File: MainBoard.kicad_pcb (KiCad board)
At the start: 4 copper layers, 110 x 100 mm, 99 parts, among them J1 USB B Mini, J5 Audio Out Port, P1 CARTRIDGE_SLOT, P2 FRONT_PANEL_CONNECTOR, P4 Multi AV Out, Q1 2SC4699, SW1 RESET, U1 S-CPU, U11 PST529D, U13 S-SMP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

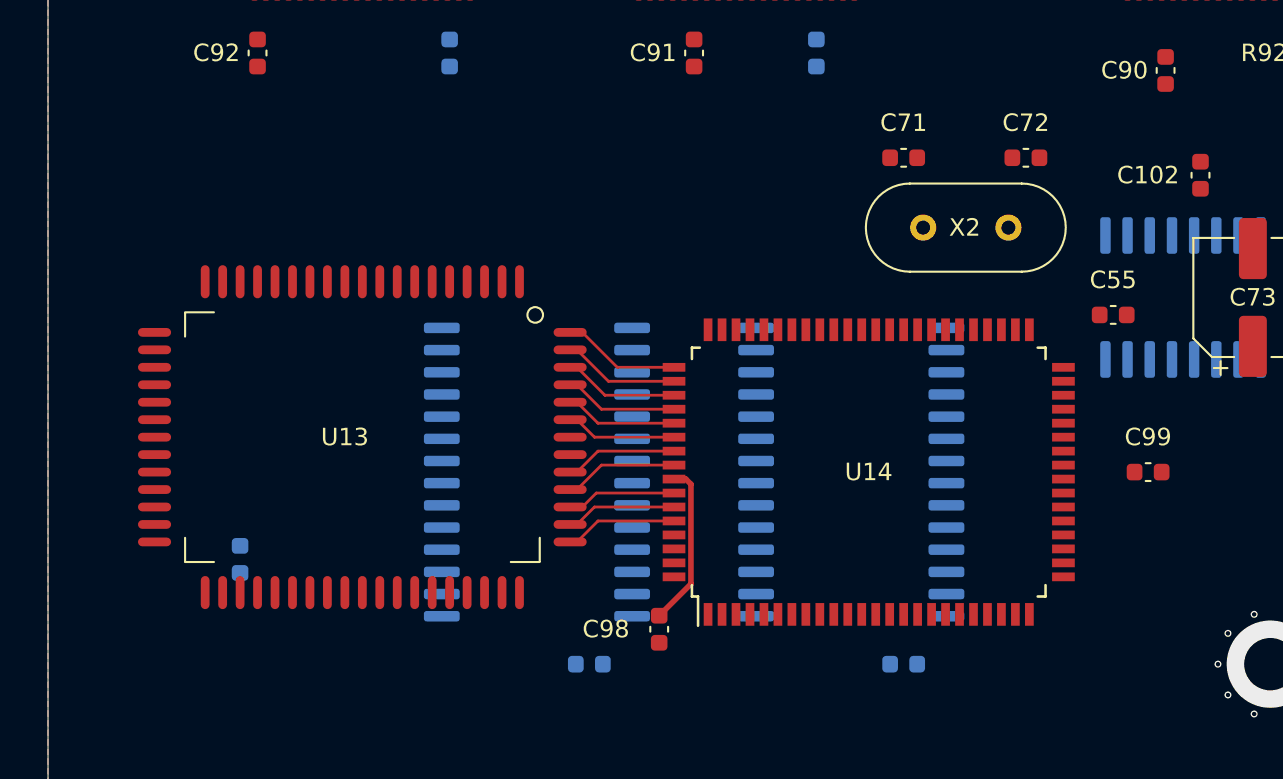
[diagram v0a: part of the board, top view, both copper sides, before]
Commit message: Sound section wiring completed
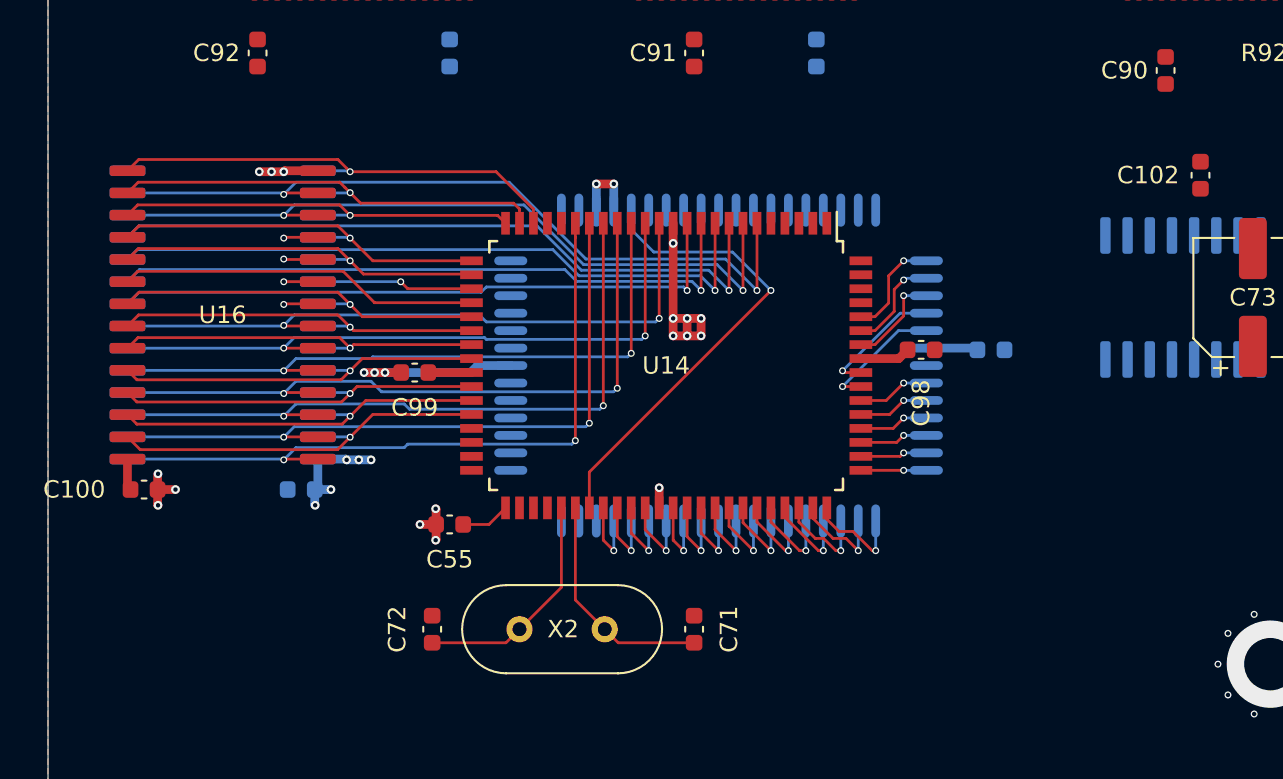
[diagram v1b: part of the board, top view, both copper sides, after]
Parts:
- C100, U16: moved to F.Cu
- U13: moved to B.Cu
- moved C97 44.6 mm to (74.0, 118.0), turned to 0 degrees
- moved C100 44.6 mm to (25.5, 126.0), turned to 180 degrees
- moved C72 43.4 mm to (42.0, 134.0), turned to 270 degrees
- moved C99 42.4 mm to (41.0, 119.3), turned to 180 degrees
- moved C55 39.8 mm to (43.0, 128.0), turned to 180 degrees
- moved U16 37.1 mm to (30.0, 116.0), turned to 180 degrees
- moved X2 36.2 mm to (47.0, 134.0), turned to 0 degrees
- moved C71 29.5 mm to (57.0, 134.0), turned to 270 degrees
- moved C98 21.9 mm to (70.0, 118.0), turned to 180 degrees
- moved U13 20.8 mm to (58.4, 118.9), turned to 90 degrees
- moved U15 20.1 mm to (30.0, 116.0)
- moved C101 19.3 mm to (34.5, 126.0)
- moved U14 13.1 mm to (55.4, 118.9), turned to 270 degrees
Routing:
- net /MD2: track 0.00 -> 44.8 mm, vias 0 -> 2
- net /MD1: track 0.00 -> 43.3 mm, vias 0 -> 2
- net /MD0: track 0.00 -> 42.1 mm, vias 0 -> 2
- net /MA0: track 0.00 -> 40.7 mm, vias 0 -> 2
- net /MA14: track 0.00 -> 40.5 mm, vias 0 -> 2
- net /MA7: track 0.00 -> 40.2 mm, vias 0 -> 2
- net /MA12: track 0.00 -> 40.2 mm, vias 0 -> 2
- net /MA6: track 0.00 -> 40.1 mm, vias 0 -> 2
- net /MA1: track 0.00 -> 39.4 mm, vias 0 -> 2
- net /MA5: track 0.00 -> 38.7 mm, vias 0 -> 2
- net /MA4: track 0.00 -> 38.4 mm, vias 0 -> 2
- net /MA3: track 0.00 -> 38.4 mm, vias 0 -> 2
- net /MA2: track 0.00 -> 38.3 mm, vias 0 -> 2
- net GND: track 0.00 -> 31.2 mm, vias 15 -> 35
- net /MD3: track 0.00 -> 27.4 mm, vias 0 -> 1
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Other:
- net class Power: trace_width 0.32 -> 0.5

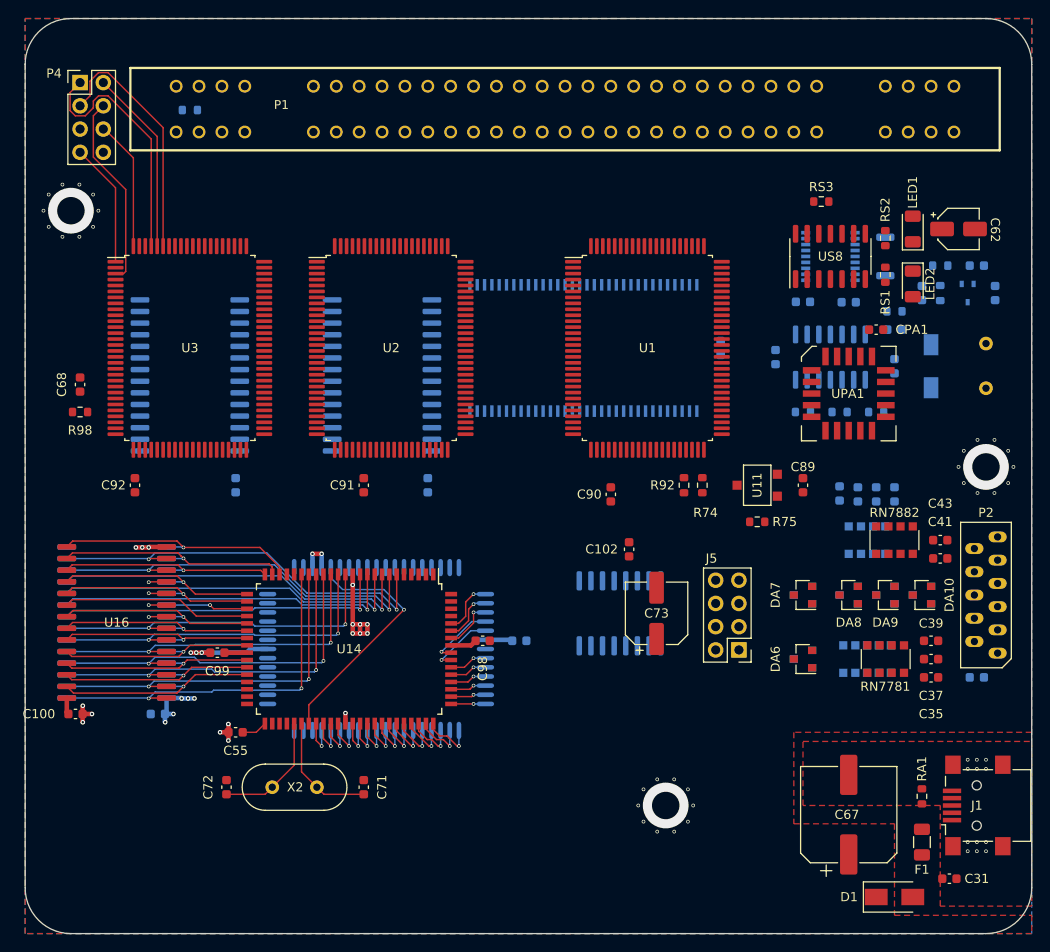
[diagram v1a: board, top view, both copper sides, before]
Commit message: Sound section connected to the main CPU now
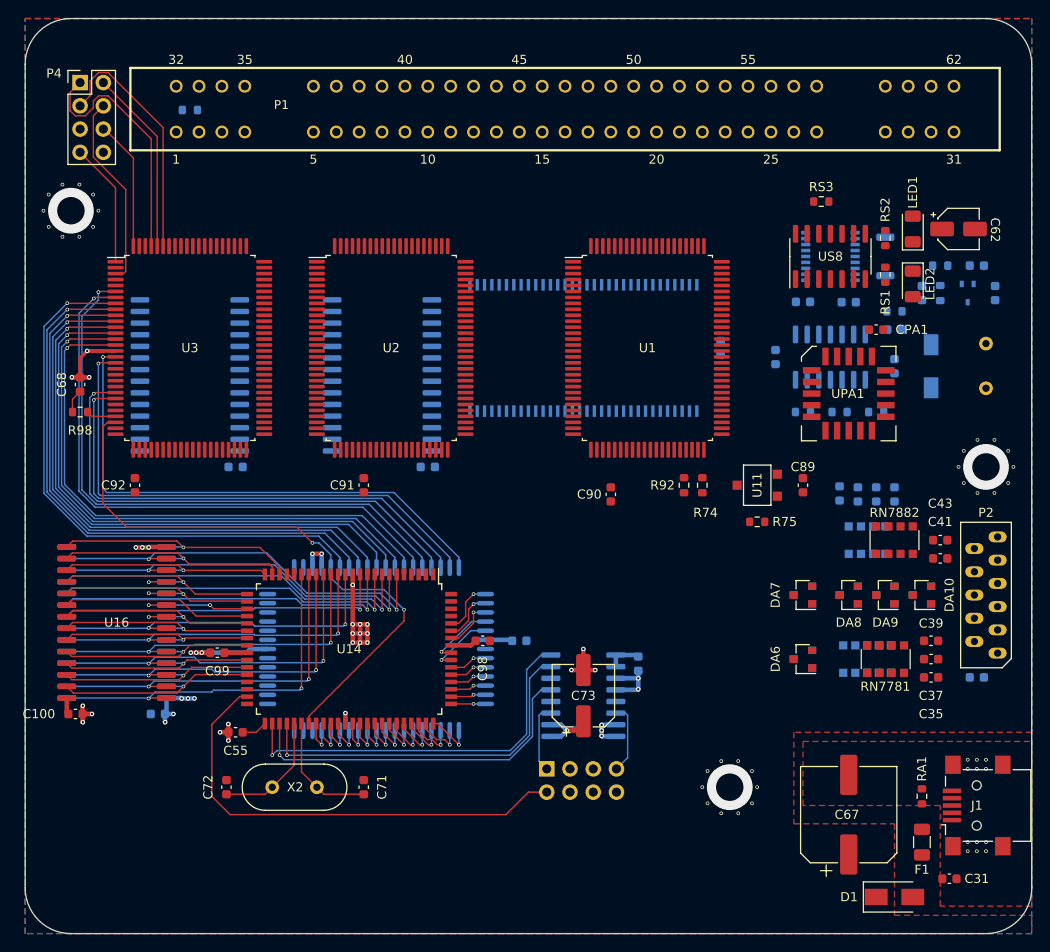
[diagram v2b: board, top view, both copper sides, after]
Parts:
- C102, J5: moved to B.Cu
- moved J5 24.7 mm to (77.0, 132.0), turned to 270 degrees
- moved C102 12.5 mm to (87.0, 120.5)
- moved C73 12.0 mm to (81.0, 124.0)
- moved U17 9.85 mm to (81.0, 124.0), turned to 180 degrees
- moved C93 2.00 mm to (43.0, 99.0), turned to 0 degrees
- moved C94 2.00 mm to (64.0, 99.0), turned to 0 degrees
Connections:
- J5 pad 1: /~MUTE -> /AUDIO_LOUT
- J5 pad 2: /AUDIO_LOUT -> /~MUTE
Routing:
- net /~PAWR: track 0.00 -> 65.6 mm, vias 0 -> 1
- net /~PARD: track 0.00 -> 64.8 mm, vias 0 -> 1
- net /D7: track 0.00 -> 63.5 mm, vias 0 -> 1
- net /D6: track 0.00 -> 63.2 mm, vias 0 -> 1
- net /D5: track 0.00 -> 63.0 mm, vias 0 -> 1
- net /D3: track 0.00 -> 62.9 mm, vias 0 -> 1
- net /D4: track 0.00 -> 62.8 mm, vias 0 -> 1
- net /D2: track 0.00 -> 62.6 mm, vias 0 -> 1
- net /D1: track 0.00 -> 62.2 mm, vias 0 -> 1
- net /D0: track 0.00 -> 62.0 mm, vias 0 -> 1
- net /PA7: track 0.00 -> 58.9 mm, vias 0 -> 1
- net /PA6: track 0.00 -> 58.5 mm, vias 0 -> 1
- net /PA1: track 0.00 -> 54.9 mm, vias 0 -> 1
- net /PA0: track 0.00 -> 54.6 mm, vias 0 -> 1
- net /~MUTE: track 0.00 -> 51.4 mm
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
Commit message: WIP, needs rewiring
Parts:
- removed C94: 0.1uF, Capacitor_SMD:C_0603_1608Metric
- C89, R75: moved to B.Cu
- U6: footprint SNES:SOP-64_10.8x28mm_P0.8mm -> SNES:SOP-64_10.9x26.5mm_P0.8mm
- moved C90 31.9 mm to (91.6, 71.0), turned to 270 degrees
- moved C95 26.2 mm to (70.5, 91.9), turned to 90 degrees
- moved U4 6.08 mm to (37.0, 83.0)
- moved R75 5.94 mm to (95.0, 101.8)
- moved C89 5.28 mm to (100.0, 102.7), turned to 0 degrees
- moved U6 4.43 mm to (82.9, 82.0)
- moved C93 4.31 mm to (46.0, 95.9), turned to 180 degrees
- moved RS3 3.16 mm to (110.0, 71.0)
- moved C62 3.00 mm to (125.0, 73.0), turned to 180 degrees
- moved LED1 3.00 mm to (120.0, 73.0)
- moved LED2 3.00 mm to (120.0, 79.0)
- moved RS1 3.00 mm to (117.0, 78.0)
- moved RS2 3.00 mm to (117.0, 74.0)
- moved UPA1 3.00 mm to (113.0, 91.0)
- moved US8 3.00 mm to (111.0, 76.0)
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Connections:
- U3 pad 34: /XIN -> /~RESET
- U8 pad 10: /XIN -> /~RESET
- US8 pad 11: /XIN -> /~RESET
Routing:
- net /PA7: track 58.9 -> 189.9 mm, vias 1 -> 6
- net /PA0: track 54.6 -> 180.2 mm, vias 1 -> 5
- net /PA1: track 54.9 -> 177.1 mm, vias 1 -> 5
- net /PA3: track 0.00 -> 109.3 mm, vias 0 -> 4
- net /PA5: track 0.00 -> 104.9 mm, vias 0 -> 3
- net /~RAMSEL: track 0.00 -> 104.9 mm, vias 0 -> 2
- net /PA2: track 0.00 -> 103.7 mm, vias 0 -> 4
- net /PA4: track 0.00 -> 101.8 mm, vias 0 -> 3
- net /~RESOUT1: track 65.9 -> 165.3 mm, vias 2 -> 4
- net /D7: track 63.5 -> 150.6 mm, vias 1 -> 4
- net /REFRESH: track 0.00 -> 84.9 mm, vias 0 -> 2
- net /PA6: track 58.5 -> 139.5 mm, vias 1 -> 4
- net /D6: track 63.2 -> 141.0 mm, vias 1 -> 4
- net /D5: track 63.0 -> 138.3 mm, vias 1 -> 4
- net /D4: track 62.8 -> 137.2 mm, vias 1 -> 4
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- added copper zone on B.Cu, net VCC
